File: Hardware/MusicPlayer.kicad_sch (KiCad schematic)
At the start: 33 parts, among them J1 USB_B_Micro, J2 AudioJack3, SW1 SW_Nidec_CAS-120A1, SW2 SW_Nidec_CAS-120A1, U1 MICROSD_SPI_OR_SDIO_CARD, U2 AMS1117, U3 ESP32-S3-WROOM-1, U4 TPS61090, U6 MCP4725xxx-xCH

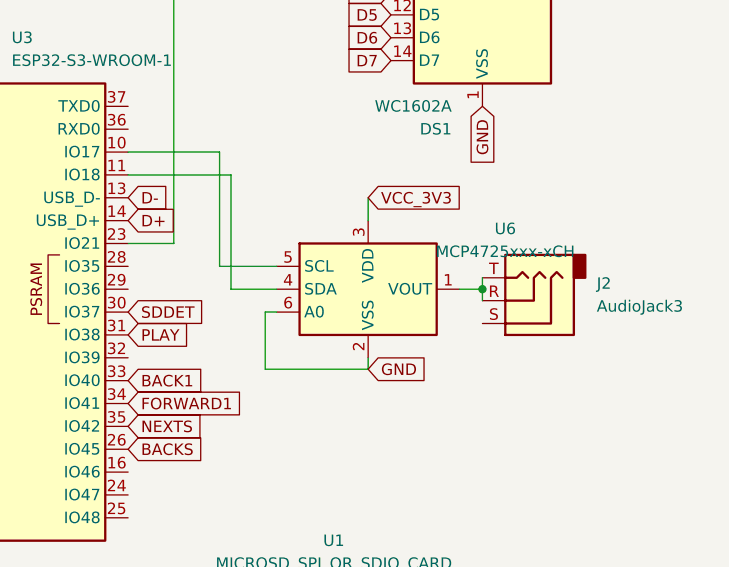
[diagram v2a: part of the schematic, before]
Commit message: temporarily removed DAC, i think i will change the MCU to one with a built in DAC
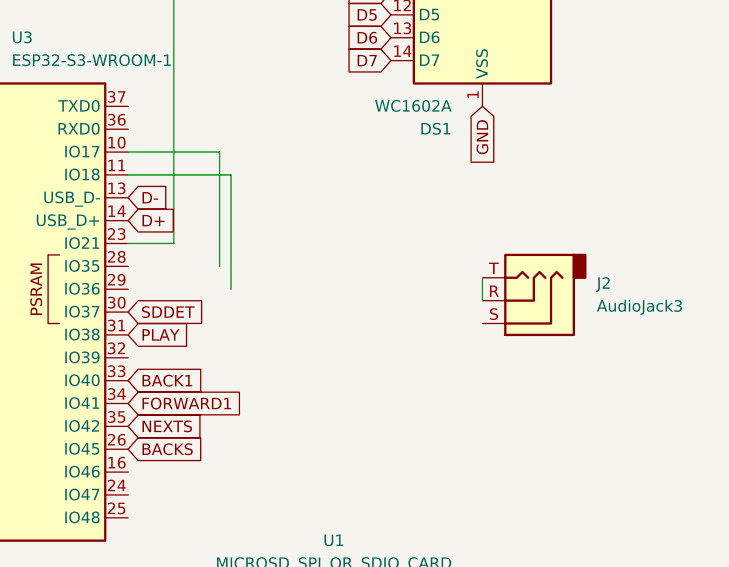
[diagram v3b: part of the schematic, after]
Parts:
- removed U6: MCP4725xxx-xCH, Package_TO_SOT_SMD:SOT-23-6, symbol Analog_DAC:MCP4725xxx-xCH
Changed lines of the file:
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@@
 	)
 	(junction
-		(at 260.35 87.63)
-		(diameter 0)
-		(color 0 0 0 0)
-	)
-	(junction
 		(at 25.4 66.04)
 		(diameter 0)
@@
 	(wire
 		(pts
-			(xy 247.65 96.52) (xy 247.65 95.25)
-		)
-		(stroke
-			(width 0)
-			(type default)
-		)
-	)
-	(wire
-		(pts
 			(xy 33.02 34.29) (xy 39.37 34.29)
 		)
@@
 	(wire
 		(pts
-			(xy 236.22 90.17) (xy 237.49 90.17)
-		)
-		(stroke
-			(width 0)
-			(type default)
-		)
-	)
-	(wire
-		(pts
 			(xy 205.74 118.11) (xy 205.74 157.48)
 		)
@@
 	(wire
 		(pts
-			(xy 232.41 87.63) (xy 237.49 87.63)
-		)
-		(stroke
-			(width 0)
-			(type default)
-		)
-	)
-	(wire
-		(pts
 			(xy 124.46 157.48) (xy 151.13 157.48)
 		)
@@
 	(wire
 		(pts
-			(xy 257.81 87.63) (xy 260.35 87.63)
-		)
-		(stroke
-			(width 0)
-			(type default)
-		)
-	)
-	(wire
-		(pts
 			(xy 36.83 137.16) (xy 29.21 137.16)
 		)
@@
 	(wire
 		(pts
-			(xy 231.14 85.09) (xy 237.49 85.09)
-		)
-		(stroke
-			(width 0)
-			(type default)
-		)
-	)
-	(wire
-		(pts
 			(xy 220.98 72.39) (xy 231.14 72.39)
 		)
@@
 	(wire
 		(pts
-			(xy 260.35 86.36) (xy 260.35 87.63)
+			(xy 260.35 86.36) (xy 260.35 88.9)
 		)
 		(stroke
@@
 	(wire
 		(pts
-			(xy 260.35 87.63) (xy 260.35 88.9)
-		)
-		(stroke
-			(width 0)
-			(type default)
-		)
-	)
-	(wire
-		(pts
 			(xy 210.82 48.26) (xy 205.74 48.26)
 		)
@@
 	(wire
 		(pts
-			(xy 236.22 96.52) (xy 247.65 96.52)
-		)
-		(stroke
-			(width 0)
-			(type default)
-		)
-	)
-	(wire
-		(pts
 			(xy 205.74 48.26) (xy 205.74 62.23)
 		)
@@
 	(wire
 		(pts
-			(xy 247.65 77.47) (xy 247.65 80.01)
-		)
-		(stroke
-			(width 0)
-			(type default)
-		)
-	)
-	(wire
-		(pts
 			(xy 67.31 88.9) (xy 74.93 88.9)
 		)
@@
 	(wire
 		(pts
-			(xy 236.22 90.17) (xy 236.22 96.52)
-		)
-		(stroke
-			(width 0)
-			(type default)
-		)
-	)
-	(wire
-		(pts
 			(xy 128.27 19.05) (xy 128.27 21.59)
 		)
@@
 		)
 	)
-	(global_label "GND"
-		(shape input)
-		(at 247.65 96.52 0)
-		(fields_autoplaced yes)
-		(effects
-			(font
-				(size 1.27 1.27)
-			)
-			(justify left)
-		)
-		(property "Intersheetrefs" "${INTERSHEET_REFS}"
-			(at 254.2343 96.52 0)
-			(effects
-				(font
-					(size 1.27 1.27)
-				)
-				(justify left)
-				(hide yes)
-			)
-		)
-	)
 	(global_label "MISO"
 		(shape input)
@@
 		)
 	)
-	(global_label "VCC_3V3"
-		(shape input)
-		(at 247.65 77.47 0)
-		(fields_autoplaced yes)
-		(effects
-			(font
-				(size 1.27 1.27)
-			)
-			(justify left)
-		)
-		(property "Intersheetrefs" "${INTERSHEET_REFS}"
-			(at 257.5161 77.47 0)
-			(effects
-				(font
-					(size 1.27 1.27)
-				)
-				(justify left)
-				(hide yes)
-			)
-		)
-	)
 	(global_label "FORWARD1"
 		(shape input)
@@
 					(unit 1)
 				)
-			)
-		)
-	)
-	(symbol
-		(lib_id "Analog_DAC:MCP4725xxx-xCH")
-		(at 247.65 87.63 0)
-		(unit 1)
-		(exclude_from_sim no)
-		(in_bom yes)
-		(on_board yes)
-		(dnp no)
-		(fields_autoplaced yes)
-		(property "Reference" "U6"
-			(at 262.89 80.9215 0)
-			(effects
-				(font
-					(size 1.27 1.27)
-				)
-			)
-		)
-		(property "Value" "MCP4725xxx-xCH"
-			(at 262.89 83.4615 0)
-			(effects
-				(font
-					(size 1.27 1.27)
-				)
-			)
-		)
-		(property "Footprint" "Package_TO_SOT_SMD:SOT-23-6"
-			(at 247.65 93.98 0)
-			(effects
-				(font
-					(size 1.27 1.27)
-				)
-				(hide yes)
-			)
-		)
-		(property "Datasheet" "http://ww1.microchip.com/downloads/en/DeviceDoc/22039d.pdf"
-			(at 247.65 87.63 0)
-			(effects
-				(font
-					(size 1.27 1.27)
-				)
-				(hide yes)
-			)
-		)
-		(property "Description" "12-bit Digital-to-Analog Converter, integrated EEPROM, I2C interface, SOT-23-6"
-			(at 247.65 87.63 0)
-			(effects
-				(font
-					(size 1.27 1.27)
-				)
-				(hide yes)
-			)
-		)
-		(pin "6"
-		)
-		(pin "2"
-		)
-		(pin "1"
-		)
-		(pin "4"
-		)
-		(pin "3"
-		)
-		(pin "5"
-		)
-		(instances
-			(project ""
-				(path "/2b7a1a48-2553-49e3-90ba-0bcdb9a91407"
-					(reference "U6")
-					(unit 1)
-				)
